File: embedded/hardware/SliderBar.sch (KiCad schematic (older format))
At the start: 10 parts

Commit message: Add step-up boost converter
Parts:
- removed REG?: HT7333, symbol nelib:HT7333
- added C?: 22uF, symbol Device:C
- added C?: C, symbol Device:C
- added D?: D_Schottky, symbol Device:D_Schottky
- added L?: 4.7uH, symbol Device:L
- added R?: 47k, symbol Device:R
- added R?: 3k, symbol Device:R
- added U?: LD1117S33TR_SOT223, Package_TO_SOT_SMD:SOT-223-3_TabPin2, symbol Regulator_Linear:LD1117S33TR_SOT223
- added U?: MT3608, symbol nelib:MT3608
- C?: value 10uF -> 100nF
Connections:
- wire segments 41 -> 66
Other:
- note added: "10V BOOST"
- note added: "3.3V REGULATOR"
- note added: "Id = sqrt(Iout * Imax)"
- note added: "Recommended:\n4.7uH - 22uH"
- note added: "Vout = 0.6 * (1 + R1 / R2)"
- moved on the sheet: C?

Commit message: Add trimmer and replace MCU with STM32F072C8T6
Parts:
- removed R?: 47k, symbol Device:R
- removed U?: STM32F030K6Tx, Package_QFP:LQFP-32_7x7mm_P0.8mm, symbol MCU_ST_STM32F0:STM32F030K6Tx
- added C?: C, symbol Device:C
- added R?: 100k, symbol Device:RTRIM
- added U?: STM32F072C8Tx, Package_QFP:LQFP-48_7x7mm_P0.5mm, symbol MCU_ST_STM32F0:STM32F072C8Tx
- C?: value C -> 22uF
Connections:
- net labels added: MOTOR_OUT1, MOTOR_OUT2
- net labels removed: AOUT1, AOUT2
- wire segments 66 -> 87
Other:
- note added: "approx\n47k"
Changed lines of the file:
@@
 $EndDescr
-$Comp
-L MCU_ST_STM32F0:STM32F030K6Tx U?
-U 1 1 5BB22E86
-P 5400 3700
-F 0 "U?" H 5800 4550 50  0000 R CNN
-F 1 "STM32F030K6Tx" H 5800 2750 50  0000 C CNN
-F 2 "Package_QFP:LQFP-32_7x7mm_P0.8mm" H 4900 2800 50  0001 R CNN
-F 3 "http://www.st.com/st-web-ui/static/active/en/resource/technical/document/datasheet/DM00088500.pdf" H 5400 3700 50  0001 C CNN
-	1    5400 3700
-	1    0    0    -1
-$EndComp
 $Comp
 L Device:C C?
@@
 L power:GND #PWR?
 U 1 1 5BB23C60
-P 9825 900
-F 0 "#PWR?" H 9825 650 50  0001 C CNN
-F 1 "GND" H 9830 727 50  0000 C CNN
-F 2 "" H 9825 900 50  0001 C CNN
-F 3 "" H 9825 900 50  0001 C CNN
-	1    9825 900
+P 9800 850
+F 0 "#PWR?" H 9800 600 50  0001 C CNN
+F 1 "GND" H 9805 677 50  0000 C CNN
+F 2 "" H 9800 850 50  0001 C CNN
+F 3 "" H 9800 850 50  0001 C CNN
+	1    9800 850
 	-1   0    0    1
 $EndComp
-$Comp
-L power:VBUS #PWR?
-U 1 1 5BB23D01
-P 9625 900
-F 0 "#PWR?" H 9625 750 50  0001 C CNN
-F 1 "VBUS" H 9640 1073 50  0000 C CNN
-F 2 "" H 9625 900 50  0001 C CNN
-F 3 "" H 9625 900 50  0001 C CNN
-	1    9625 900
-	1    0    0    -1
-$EndComp
-Wire Wire Line
-	9825 900  9825 1000
-Wire Wire Line
-	9825 1000 10250 1000
-Wire Wire Line
-	9625 900  9625 1200
-Wire Wire Line
-	9625 1200 10250 1200
 Text GLabel 10175 2050 0    50   Input ~ 0
-AOUT1
+MOTOR_OUT1
 Text GLabel 10175 2150 0    50   Input ~ 0
-AOUT2
+MOTOR_OUT2
 Text GLabel 10200 2725 0    50   Input ~ 0
 POT
@@
 Connection ~ 2450 6900
 Text GLabel 2950 5450 2    50   Input ~ 0
-AOUT1
+MOTOR_OUT1
 Text GLabel 2950 5650 2    50   Input ~ 0
-AOUT2
+MOTOR_OUT2
 Wire Wire Line
 	2950 5450 2900 5450
@@
 	1    0    0    -1
 $EndComp
-$Comp
-L power:+3.3V #PWR?
-U 1 1 5BC35A77
-P 2950 1550
-F 0 "#PWR?" H 2950 1400 50  0001 C CNN
-F 1 "+3.3V" H 2965 1723 50  0000 C CNN
-F 2 "" H 2950 1550 50  0001 C CNN
-F 3 "" H 2950 1550 50  0001 C CNN
-	1    2950 1550
-	1    0    0    -1
-$EndComp
 Wire Wire Line
 	2750 1650 2950 1650
@@
 $Comp
 L Device:R R?
-U 1 1 5BC45001
-P 5900 2050
-F 0 "R?" V 5693 2050 50  0000 C CNN
-F 1 "47k" V 5784 2050 50  0000 C CNN
-F 2 "" V 5830 2050 50  0001 C CNN
-F 3 "~" H 5900 2050 50  0001 C CNN
-	1    5900 2050
-	0    1    1    0
-$EndComp
-$Comp
-L Device:R R?
 U 1 1 5BC47906
 P 5900 2350
@@
 P 6300 1850
 F 0 "C?" H 6185 1804 50  0000 R CNN
-F 1 "C" H 6185 1895 50  0000 R CNN
+F 1 "22uF" H 6185 1895 50  0000 R CNN
 F 2 "" H 6338 1700 50  0001 C CNN
 F 3 "~" H 6300 1850 50  0001 C CNN
@@
 Wire Wire Line
 	6300 2000 6300 2050
+$Comp
+L Device:RTRIM R?
+U 1 1 5BCA1C5C
+P 5900 2050
+F 0 "R?" V 5660 2050 50  0000 C CNN
+F 1 "100k" V 5751 2050 50  0000 C CNN
+F 2 "" V 5830 2050 50  0001 C CNN
+F 3 "~" H 5900 2050 50  0001 C CNN
+	1    5900 2050
+	0    1    1    0
+$EndComp
+Text Notes 5750 1750 0    50   ~ 0
+approx\n47k
+$Comp
+L power:+3V3 #PWR?
+U 1 1 5BCA296C
+P 2950 1550
+F 0 "#PWR?" H 2950 1400 50  0001 C CNN
+F 1 "+3V3" H 2965 1723 50  0000 C CNN
+F 2 "" H 2950 1550 50  0001 C CNN
+F 3 "" H 2950 1550 50  0001 C CNN
+	1    2950 1550
+	1    0    0    -1
+$EndComp
+$Comp
+L power:+3V3 #PWR?
+U 1 1 5BCA2B2D
+P 6750 2800
+F 0 "#PWR?" H 6750 2650 50  0001 C CNN
+F 1 "+3V3" H 6765 2973 50  0000 C CNN
+F 2 "" H 6750 2800 50  0001 C CNN
+F 3 "" H 6750 2800 50  0001 C CNN
+	1    6750 2800
+	1    0    0    -1
+$EndComp
+Wire Wire Line
+	10250 1000 9800 1000
+Wire Wire Line
+	9800 1000 9800 850
+$Comp
+L power:+3V3 #PWR?
+U 1 1 5BCA6950
+P 9550 850
+F 0 "#PWR?" H 9550 700 50  0001 C CNN
+F 1 "+3V3" H 9565 1023 50  0000 C CNN
+F 2 "" H 9550 850 50  0001 C CNN
+F 3 "" H 9550 850 50  0001 C CNN
+	1    9550 850
+	1    0    0    -1
+$EndComp
+Wire Wire Line
+	9550 850  9550 1200
+Wire Wire Line
+	9550 1200 10250 1200
+Wire Wire Line
+	6750 2800 6750 2900
+Wire Wire Line
+	6650 3000 6650 2900
+Wire Wire Line
+	6650 2900 6750 2900
+Connection ~ 6750 2900
+Wire Wire Line
+	6750 2900 6750 3000
+Wire Wire Line
+	6550 3000 6550 2900
+Wire Wire Line
+	6550 2900 6650 2900
+Connection ~ 6650 2900
+$Comp
+L power:GND #PWR?
+U 1 1 5BCAB682
+P 6550 6200
+F 0 "#PWR?" H 6550 5950 50  0001 C CNN
+F 1 "GND" H 6555 6027 50  0000 C CNN
+F 2 "" H 6550 6200 50  0001 C CNN
+F 3 "" H 6550 6200 50  0001 C CNN
+	1    6550 6200
+	1    0    0    -1
+$EndComp
+Wire Wire Line
+	6550 6200 6550 6100
+Wire Wire Line
+	6650 6000 6650 6100
+Wire Wire Line
+	6650 6100 6550 6100
+Connection ~ 6550 6100
+Wire Wire Line
+	6550 6100 6550 6000
+$Comp
+L MCU_ST_STM32F0:STM32F072C8Tx U?
+U 1 1 5BCADD80
+P 6750 4500
+F 0 "U?" H 6200 5950 50  0000 C CNN
+F 1 "STM32F072C8Tx" H 7350 5950 50  0000 C CNN
+F 2 "Package_QFP:LQFP-48_7x7mm_P0.5mm" H 6150 3100 50  0001 R CNN
+F 3 "http://www.st.com/st-web-ui/static/active/en/resource/technical/document/datasheet/DM00090510.pdf" H 6750 4500 50  0001 C CNN
+	1    6750 4500
+	1    0    0    -1
+$EndComp
+Wire Wire Line
+	6650 6100 6750 6100
+Wire Wire Line
+	6750 6100 6750 6000
+Connection ~ 6650 6100
+Wire Wire Line
+	6750 6100 6850 6100
+Wire Wire Line
+	6850 6100 6850 6000
+Connection ~ 6750 6100
+Wire Wire Line
+	6750 2900 6850 2900
+Wire Wire Line
+	6850 2900 6850 3000
+Wire Wire Line
+	6850 2900 6950 2900
+Wire Wire Line
+	6950 2900 6950 3000
+Connection ~ 6850 2900
+$Comp
+L power:GND #PWR?
+U 1 1 5BCB754A
+P 5600 3600
+F 0 "#PWR?" H 5600 3350 50  0001 C CNN
+F 1 "GND" H 5605 3427 50  0000 C CNN
+F 2 "" H 5600 3600 50  0001 C CNN
+F 3 "" H 5600 3600 50  0001 C CNN
+	1    5600 3600
+	1    0    0    -1
+$EndComp
+$Comp
+L Device:C C?
+U 1 1 5BCB759C
+P 5600 3350
+F 0 "C?" H 5715 3396 50  0000 L CNN
+F 1 "C" H 5715 3305 50  0000 L CNN
+F 2 "" H 5638 3200 50  0001 C CNN
+F 3 "~" H 5600 3350 50  0001 C CNN
+	1    5600 3350
+	1    0    0    -1
+$EndComp
+Wire Wire Line
+	6050 3200 5600 3200
+Wire Wire Line
+	5500 3200 5600 3200
+Connection ~ 5600 3200
+Text GLabel 5500 3200 0    50   Input ~ 0
+NRST
+Wire Wire Line
+	5600 3600 5600 3500
+Text GLabel 7350 5600 2    50   Input ~ 0
+SWDIO
+Text GLabel 7350 5700 2    50   Input ~ 0
+SWCLK
+Text GLabel 6050 4300 0    50   Input ~ 0
+POT
 $EndSCHEMATC

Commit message: Change Voltage regulator to MIC5205
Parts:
- removed C?: 10uF, symbol Device:C
- removed C?: 100nF, symbol Device:C
- removed U?: LD1117S33TR_SOT223, Package_TO_SOT_SMD:SOT-223-3_TabPin2, symbol Regulator_Linear:LD1117S33TR_SOT223
- added C1, C2: 10uF, symbol Device:C_Small
- added C3: 470pF, symbol Device:C_Small
- added U1: MIC5205-3.3YM5, Package_TO_SOT_SMD:SOT-23-5, symbol Regulator_Linear:MIC5205-3.3YM5
- gave numbers to parts that had none: 15
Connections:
- wire segments 87 -> 94
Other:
- moved on the sheet: C5, C6, D1, L1, R1, R2, U3

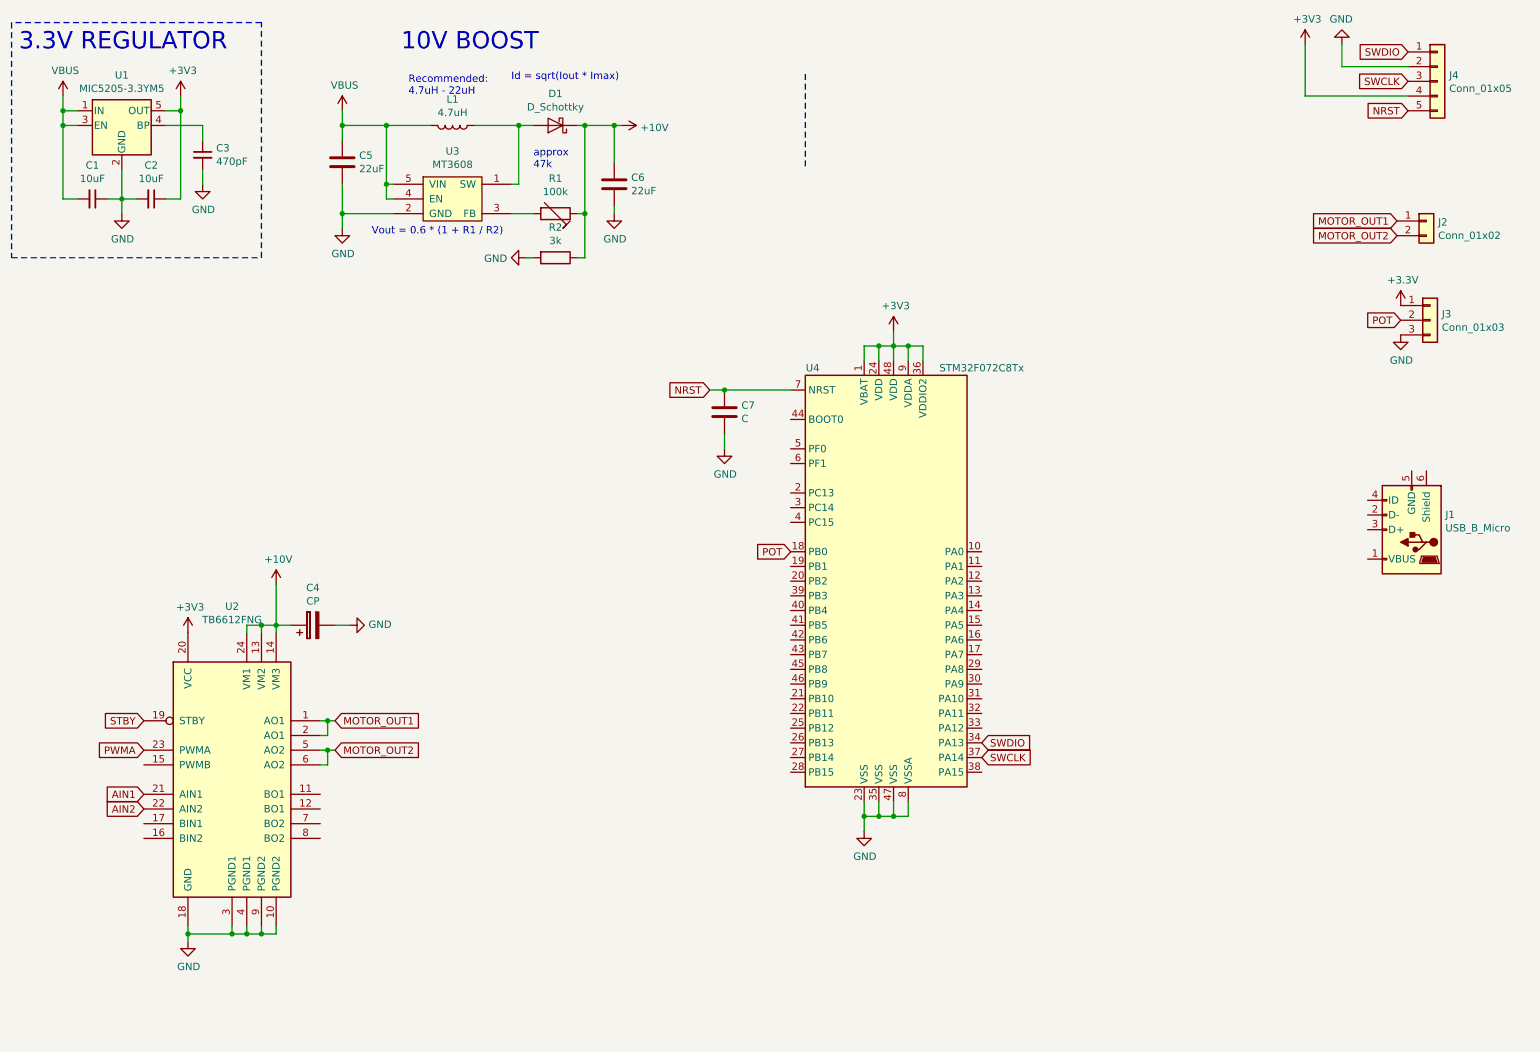
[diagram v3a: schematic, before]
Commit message: Fix GND rotation
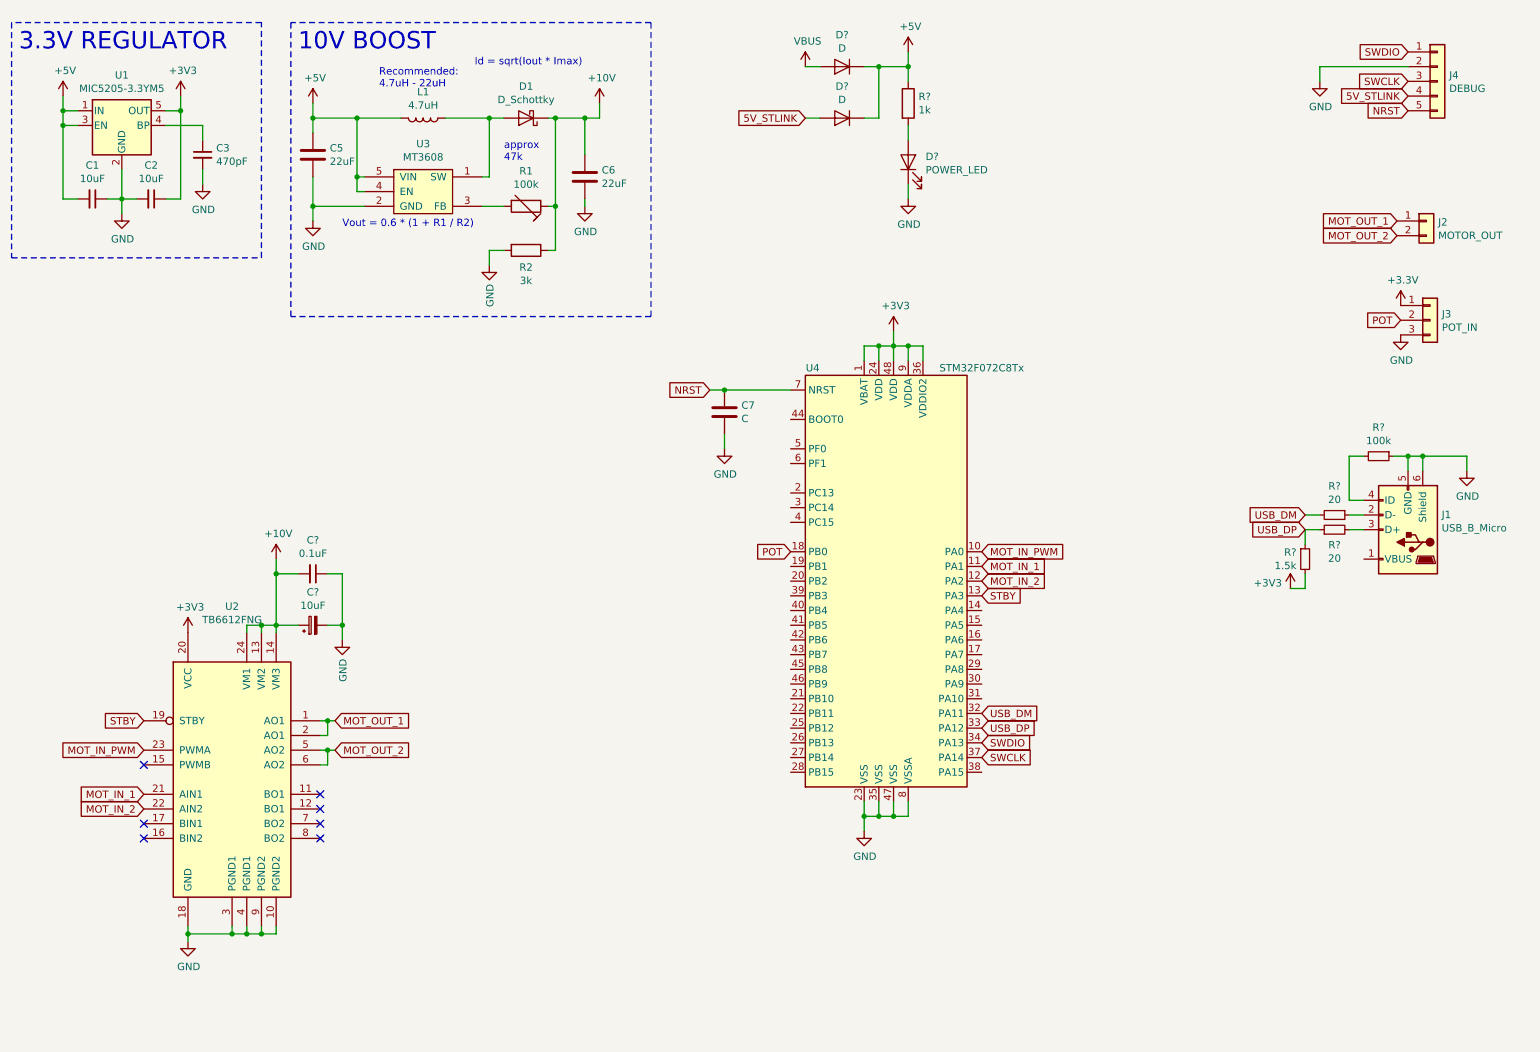
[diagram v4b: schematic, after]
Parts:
- removed C4: CP, symbol Device:CP
- added C?: 10uF, symbol Device:CP_Small
- added C?: 0.1uF, symbol Device:C_Small
- added D? (x2): D, symbol Device:D
- added D?: POWER_LED, symbol Device:LED
- added R?: 1k, symbol Device:R
- added R? (x2): 20, symbol Device:R_Small
- added R?: 1.5k, symbol Device:R_Small
- added R?: 100k, symbol Device:R_Small
- J2: value Conn_01x02 -> MOTOR_OUT
- J3: value Conn_01x03 -> POT_IN
- J4: value Conn_01x05 -> DEBUG
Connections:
- net AIN1 is gone; now on net MOT_IN_1: U2.21 (AIN1)
- net AIN2 is gone; now on net MOT_IN_2: U2.22 (AIN2)
- net PWMA is gone; now on net MOT_IN_PWM: U2.23 (PWMA)
- net +10V: now also C?.1, C?.2
- net +3V3: now also R?.2; no longer J4.4 (Pin_4)
- net GND: now also J1.5 (GND), J1.6 (Shield), C?.1, C?.2, D?.1 (K), R?.1
- net STBY: now also U4.13 (PA3)
- net VBUS: now also D?.2 (A); no longer C1.2, C5.1, L1.2, U1.1 (IN), U1.3 (EN), U3.4 (EN), U3.5 (VIN)
- net at J1.2 (D-): now also R?.1
- net at J1.3 (D+): now also R?.2
- net at J1.4 (ID): now also R?.2
- net MOT_IN_PWM: now reaches U4.10 (PA0)
- net MOT_IN_1: now reaches U4.11 (PA1)
- net MOT_IN_2: now reaches U4.12 (PA2)
- net USB_DM: now reaches U4.32 (PA11)
- net USB_DM: now also R?.2
- net USB_DP: now reaches U4.33 (PA12)
- net USB_DP: now also R?.1, R?.1
- net MOTOR_OUT1 renamed MOT_OUT_1
- net MOTOR_OUT2 renamed MOT_OUT_2
- new net: D?.2 (A), R?.2
- new net +5V: C1.2, C5.1, D?.1 (K), D?.1 (K), L1.2, R?.1, U1.1 (IN), U1.3 (EN), U3.4 (EN), U3.5 (VIN)
- new net 5V_STLINK: D?.2 (A), J4.4 (Pin_4)
- no-connect marks 0 -> 7
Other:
- moved on the sheet: C5, C6, D1, J1, L1, R1, R2, U3

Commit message: Fix schottky diodes, finish schematic
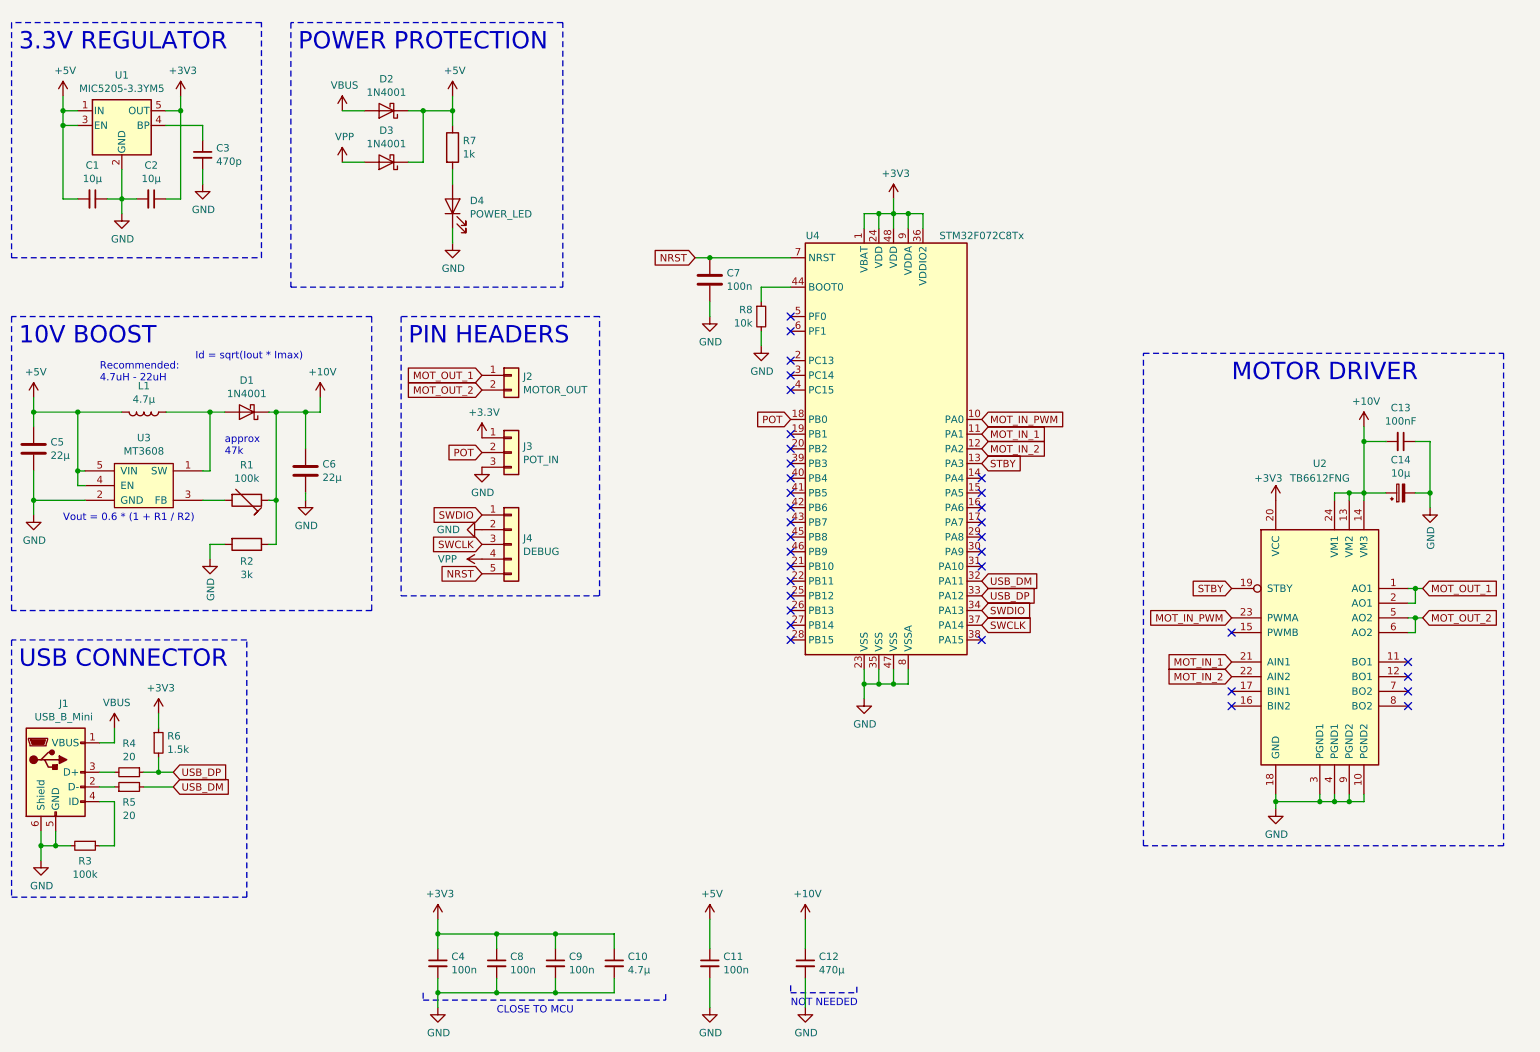
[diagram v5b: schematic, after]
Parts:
- removed D? (x2): D, symbol Device:D
- removed J1: USB_B_Micro, symbol Connector:USB_B_Micro
- added C10: 4.7µ, Capacitor_SMD:C_1206_3216Metric_Pad1.42x1.75mm_HandSolder, symbol Device:C_Small
- added C11, C4, C8, C9: 100n, Capacitor_SMD:C_1206_3216Metric_Pad1.42x1.75mm_HandSolder, symbol Device:C_Small
- added C12: 470µ, Capacitor_SMD:C_1206_3216Metric_Pad1.42x1.75mm_HandSolder, symbol Device:C_Small
- added D2, D3: 1N4001, Diode_SMD:D_SMA_Handsoldering, symbol Device:D_Schottky
- added J1: USB_B_Mini, Connector_USB:USB_Mini-B_Lumberg_2486_01_Horizontal, symbol Connector:USB_B_Mini
- added R8: 10k, Resistor_SMD:R_1206_3216Metric_Pad1.42x1.75mm_HandSolder, symbol Device:R_Small
- C1, C2: value 10uF -> 10µ; footprint (none) -> Capacitor_SMD:C_1206_3216Metric_Pad1.42x1.75mm_HandSolder
- C13: renamed from C?; value 0.1uF -> 100nF; footprint (none) -> Capacitor_SMD:C_1206_3216Metric_Pad1.42x1.75mm_HandSolder
- C14: renamed from C?; value 10uF -> 10µ; footprint (none) -> Capacitor_Tantalum_SMD:CP_EIA-7343-15_Kemet-W
- C3: value 470pF -> 470p; footprint (none) -> Capacitor_SMD:C_1206_3216Metric_Pad1.42x1.75mm_HandSolder
- C5, C6: value 22uF -> 22µ; footprint (none) -> Capacitor_SMD:C_1206_3216Metric_Pad1.42x1.75mm_HandSolder
- C7: value C -> 100n; footprint (none) -> Capacitor_SMD:C_1206_3216Metric_Pad1.42x1.75mm_HandSolder
- D1: value D_Schottky -> 1N4001; footprint (none) -> Diode_SMD:D_SMA_Handsoldering
- D4: renamed from D?; footprint (none) -> LED_SMD:LED_1206_3216Metric_Pad1.42x1.75mm_HandSolder
- J2: footprint (none) -> Connector_JST:JST_SH_SM02B-SRSS-TB_1x02-1MP_P1.00mm_Horizontal
- J3: footprint (none) -> Connector_JST:JST_SH_SM03B-SRSS-TB_1x03-1MP_P1.00mm_Horizontal
- J4: footprint (none) -> Connector_JST:JST_SH_SM05B-SRSS-TB_1x05-1MP_P1.00mm_Horizontal
- L1: value 4.7uH -> 4.7µ; footprint (none) -> Inductor_SMD:L_1206_3216Metric_Pad1.42x1.75mm_HandSolder
- R1: footprint (none) -> ab2_passive:AB2_POT_TRIM
- R2: footprint (none) -> Resistor_SMD:R_1206_3216Metric_Pad1.42x1.75mm_HandSolder
- R3, R4, R5, R6, R7: renamed from R?; footprint (none) -> Resistor_SMD:R_1206_3216Metric_Pad1.42x1.75mm_HandSolder
- U3: footprint (none) -> Package_TO_SOT_SMD:SOT-23-6_Handsoldering
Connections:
- net +10V: now also C12.1
- net +3V3: now also R6.1, C10.1, C4.1, C8.1, C9.1; no longer R6.2
- net +5V: now also C11.1, D2.1 (K), D3.1 (K)
- net GND: now also R3.2, C10.2, C11.2, C12.2, C4.2, C8.2, C9.2, J1.5 (GND), J1.6 (Shield), R8.2; no longer R3.1
- net USB_DM: now also R5.2; no longer R4.2
- net USB_DP: now also R4.1, R6.2; no longer R5.1, R6.1
- net VBUS: now also D2.2 (A), J1.1 (VBUS)
- net at U4.44 (BOOT0): now also R8.1
- net 5V_STLINK renamed VPP
- net VPP: now also D3.2 (A)
- new net: J1.3 (D+), R4.2
- new net: J1.2 (D-), R5.1
- new net: J1.4 (ID), R3.1
- no-connect marks 7 -> 35
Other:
- note added: "CLOSE TO MCU"
- note added: "MOTOR DRIVER"
- note added: "NOT NEEDED"
- note added: "PIN HEADERS"
- note added: "POWER PROTECTION"
- note added: "USB CONNECTOR"
- moved on the sheet: C13, C14, C5, C6, C7, D1, D4, J2, J3, J4, L1, R1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
